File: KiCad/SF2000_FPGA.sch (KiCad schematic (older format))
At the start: 23 parts, among them J10 Conn_02x01, J11 Conn_02x01, J12 Conn_01x01, J3 Conn_02x03_Odd_Even, J4 Conn_02x01, J8 Conn_02x01, J9 Conn_02x01, U28 GW1N-UV9LQ144, U3 74LVC2G14, U8 T8Q144C3

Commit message: Fixed enumeration of single resistors references in ascending order
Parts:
- R3: renamed from R2; value 33Ω -> 33
- R4: renamed from R6; value 220 -> 330
- renumbered R11 to R10, R13 to R11, R12 to R5, R9 to R6, R4 to R8, R5 to R9
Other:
- moved on the sheet: R10, R11, R5, R6
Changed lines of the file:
@@
 P 7500 1850
 AR Path="/62517BB4" Ref="R?"  Part="1"
-AR Path="/620D263D/62517BB4" Ref="R4"  Part="1"
-F 0 "R4" H 7559 1896 50  0000 L CNN
+AR Path="/620D263D/62517BB4" Ref="R8"  Part="1"
+F 0 "R8" H 7559 1896 50  0000 L CNN
 F 1 "10k" H 7559 1805 50  0000 L CNN
 F 2 "Resistor_SMD:R_0805_2012Metric_Pad1.15x1.40mm_HandSolder" H 7500 1850 50  0001 C CNN
@@
 P 8000 2050
 AR Path="/62519236" Ref="R?"  Part="1"
-AR Path="/620D263D/62519236" Ref="R5"  Part="1"
-F 0 "R5" V 8100 2000 50  0000 L CNN
+AR Path="/620D263D/62519236" Ref="R9"  Part="1"
+F 0 "R9" V 8100 2000 50  0000 L CNN
 F 1 "10k" V 7900 2000 50  0000 L CNN
 F 2 "Resistor_SMD:R_0805_2012Metric_Pad1.15x1.40mm_HandSolder" H 8000 2050 50  0001 C CNN
@@
 P 9900 3050
 AR Path="/625C5BBC" Ref="R?"  Part="1"
-AR Path="/620D263D/625C5BBC" Ref="R6"  Part="1"
-F 0 "R6" V 10000 3000 50  0000 L CNN
-F 1 "220" V 9800 3000 50  0000 L CNN
+AR Path="/620D263D/625C5BBC" Ref="R4"  Part="1"
+F 0 "R4" V 10000 3000 50  0000 L CNN
+F 1 "330" V 9800 3000 50  0000 L CNN
 F 2 "Resistor_SMD:R_0805_2012Metric_Pad1.15x1.40mm_HandSolder" H 9900 3050 50  0001 C CNN
 F 3 "~" H 9900 3050 50  0001 C CNN
@@
 P -7250 4900
 AR Path="/6302BBCE" Ref="R?"  Part="1"
-AR Path="/620D263D/6302BBCE" Ref="R2"  Part="1"
-F 0 "R2" V -7350 4800 50  0000 L CNN
-F 1 "33Ω" V -7150 4850 50  0000 L CNN
+AR Path="/620D263D/6302BBCE" Ref="R3"  Part="1"
+F 0 "R3" V -7350 4800 50  0000 L CNN
+F 1 "33" V -7250 4850 50  0000 L CNN
 F 2 "Resistor_SMD:R_0805_2012Metric_Pad1.15x1.40mm_HandSolder" H -7250 4900 50  0001 C CNN
 F 3 "~" H -7250 4900 50  0001 C CNN
@@
 TDI
 NoConn ~ 7750 3200
-Text GLabel 10300 4050 3    50   Input ~ 0
+Text GLabel 10750 4050 3    50   Input ~ 0
 ACTIVE
-Text GLabel 10300 3850 1    50   Input ~ 0
-3V3
-$Comp
-L Device:R_Small R?
-U 1 1 63189641
-P 10300 3950
-AR Path="/63189641" Ref="R?"  Part="1"
-AR Path="/620D263D/63189641" Ref="R13"  Part="1"
-F 0 "R13" V 10400 3900 50  0000 L CNN
-F 1 "10k" V 10200 3900 50  0000 L CNN
-F 2 "Resistor_SMD:R_0805_2012Metric_Pad1.15x1.40mm_HandSolder" H 10300 3950 50  0001 C CNN
-F 3 "~" H 10300 3950 50  0001 C CNN
-	1    10300 3950
-	1    0    0    -1
-$EndComp
-Text GLabel 9950 3850 1    50   Input ~ 0
+Text GLabel 10750 3850 1    50   Input ~ 0
+3V3
+Text GLabel 9700 3850 1    50   Input ~ 0
 3V3
 $Comp
 L Device:R_Small R?
 U 1 1 6314ED20
-P 9950 3950
+P 9700 3950
 AR Path="/6314ED20" Ref="R?"  Part="1"
-AR Path="/620D263D/6314ED20" Ref="R12"  Part="1"
-F 0 "R12" V 10050 3900 50  0000 L CNN
-F 1 "10k" V 9850 3900 50  0000 L CNN
-F 2 "Resistor_SMD:R_0805_2012Metric_Pad1.15x1.40mm_HandSolder" H 9950 3950 50  0001 C CNN
-F 3 "~" H 9950 3950 50  0001 C CNN
-	1    9950 3950
-	1    0    0    -1
-$EndComp
-Text GLabel 9600 3850 1    50   Input ~ 0
-3V3
-$Comp
-L Device:R_Small R?
-U 1 1 68C712CB
-P 10650 3950
-AR Path="/68C712CB" Ref="R?"  Part="1"
-AR Path="/620D263D/68C712CB" Ref="R11"  Part="1"
-F 0 "R11" V 10750 3900 50  0000 L CNN
-F 1 "100k" V 10550 3850 50  0000 L CNN
-F 2 "Resistor_SMD:R_0805_2012Metric_Pad1.20x1.40mm_HandSolder" H 10650 3950 50  0001 C CNN
-F 3 "~" H 10650 3950 50  0001 C CNN
-	1    10650 3950
-	1    0    0    -1
-$EndComp
-Text GLabel 10650 3850 1    50   Input ~ 0
-3V3
-Text GLabel 10650 4050 3    50   Input ~ 0
+AR Path="/620D263D/6314ED20" Ref="R5"  Part="1"
+F 0 "R5" V 9800 3900 50  0000 L CNN
+F 1 "10k" V 9600 3900 50  0000 L CNN
+F 2 "Resistor_SMD:R_0805_2012Metric_Pad1.15x1.40mm_HandSolder" H 9700 3950 50  0001 C CNN
+F 3 "~" H 9700 3950 50  0001 C CNN
+	1    9700 3950
+	1    0    0    -1
+$EndComp
+Text GLabel 10050 3850 1    50   Input ~ 0
+3V3
+Text GLabel 10400 3850 1    50   Input ~ 0
+3V3
+Text GLabel 10400 4050 3    50   Input ~ 0
 CRESET_N
 Text GLabel -6750 5100 0    50   Input ~ 0
@@
 	10350 5600 10250 5600
 NoConn ~ -6750 5200
-Text GLabel 9600 4050 3    50   Input ~ 0
+Text GLabel 10050 4050 3    50   Input ~ 0
 JP2
 $Comp
 L Device:R_Small R?
 U 1 1 626987D6
-P 9600 3950
+P 10050 3950
 AR Path="/626987D6" Ref="R?"  Part="1"
-AR Path="/620D263D/626987D6" Ref="R9"  Part="1"
-F 0 "R9" V 9700 3900 50  0000 L CNN
-F 1 "10k" V 9500 3900 50  0000 L CNN
-F 2 "Resistor_SMD:R_0805_2012Metric_Pad1.15x1.40mm_HandSolder" H 9600 3950 50  0001 C CNN
-F 3 "~" H 9600 3950 50  0001 C CNN
-	1    9600 3950
+AR Path="/620D263D/626987D6" Ref="R6"  Part="1"
+F 0 "R6" V 10150 3900 50  0000 L CNN
+F 1 "10k" V 9950 3900 50  0000 L CNN
+F 2 "Resistor_SMD:R_0805_2012Metric_Pad1.15x1.40mm_HandSolder" H 10050 3950 50  0001 C CNN
+F 3 "~" H 10050 3950 50  0001 C CNN
+	1    10050 3950
 	1    0    0    -1
 $EndComp
@@
 Wire Wire Line
 	-7350 4900 -7350 5050
-Text GLabel 9950 4050 3    50   Input ~ 0
+Text GLabel 9700 4050 3    50   Input ~ 0
 SPI_SS
 Text GLabel 7750 3100 2    50   Input ~ 0
 SPI_SS
+$Comp
+L Device:R_Small R?
+U 1 1 63189641
+P 10750 3950
+AR Path="/63189641" Ref="R?"  Part="1"
+AR Path="/620D263D/63189641" Ref="R11"  Part="1"
+F 0 "R11" V 10850 3900 50  0000 L CNN
+F 1 "10k" V 10650 3900 50  0000 L CNN
+F 2 "Resistor_SMD:R_0805_2012Metric_Pad1.15x1.40mm_HandSolder" H 10750 3950 50  0001 C CNN
+F 3 "~" H 10750 3950 50  0001 C CNN
+	1    10750 3950
+	1    0    0    -1
+$EndComp
+$Comp
+L Device:R_Small R?
+U 1 1 68C712CB
+P 10400 3950
+AR Path="/68C712CB" Ref="R?"  Part="1"
+AR Path="/620D263D/68C712CB" Ref="R10"  Part="1"
+F 0 "R10" V 10500 3900 50  0000 L CNN
+F 1 "100k" V 10300 3850 50  0000 L CNN
+F 2 "Resistor_SMD:R_0805_2012Metric_Pad1.20x1.40mm_HandSolder" H 10400 3950 50  0001 C CNN
+F 3 "~" H 10400 3950 50  0001 C CNN
+	1    10400 3950
+	1    0    0    -1
+$EndComp
 $EndSCHEMATC

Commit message: Add TLV74312PDBV 1.2V voltage regulator, change C7 value to 2.2uF
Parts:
- renumbered U3 to U19
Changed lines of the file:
@@
 GND
 $Comp
-L SF2000:74LVC2G14 U3
+L SF2000:74LVC2G14 U19
 U 1 1 623FD973
 P 9250 2250
-F 0 "U3" H 9250 2765 50  0000 C CNN
+F 0 "U19" H 9250 2765 50  0000 C CNN
 F 1 "74LVC2G14" H 9250 2674 50  0000 C CNN
 F 2 "Package_SO:TSOP-6_1.65x3.05mm_P0.95mm" H 9750 3200 50  0001 C CNN

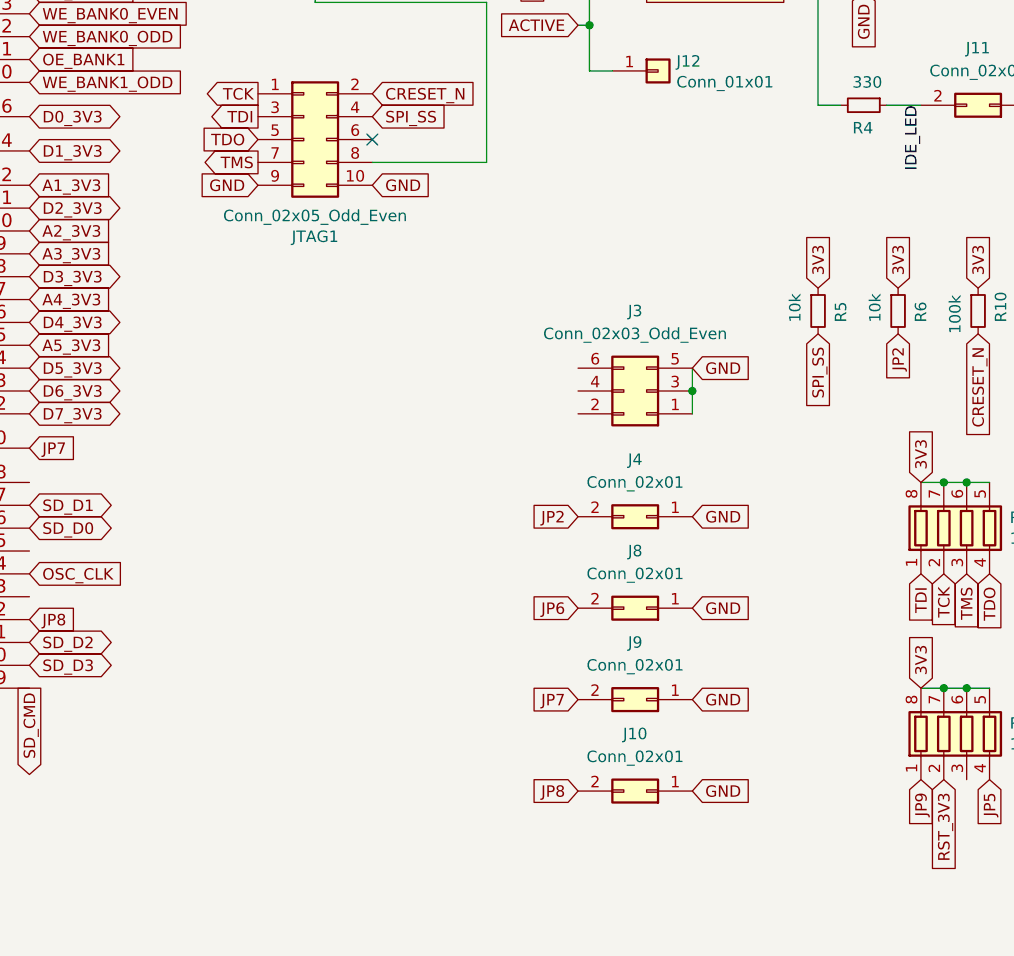
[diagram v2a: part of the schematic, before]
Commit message: Add SPI NOR Flash 8 Mbit in SOIC-8 package (AT25SF081B-SSH)
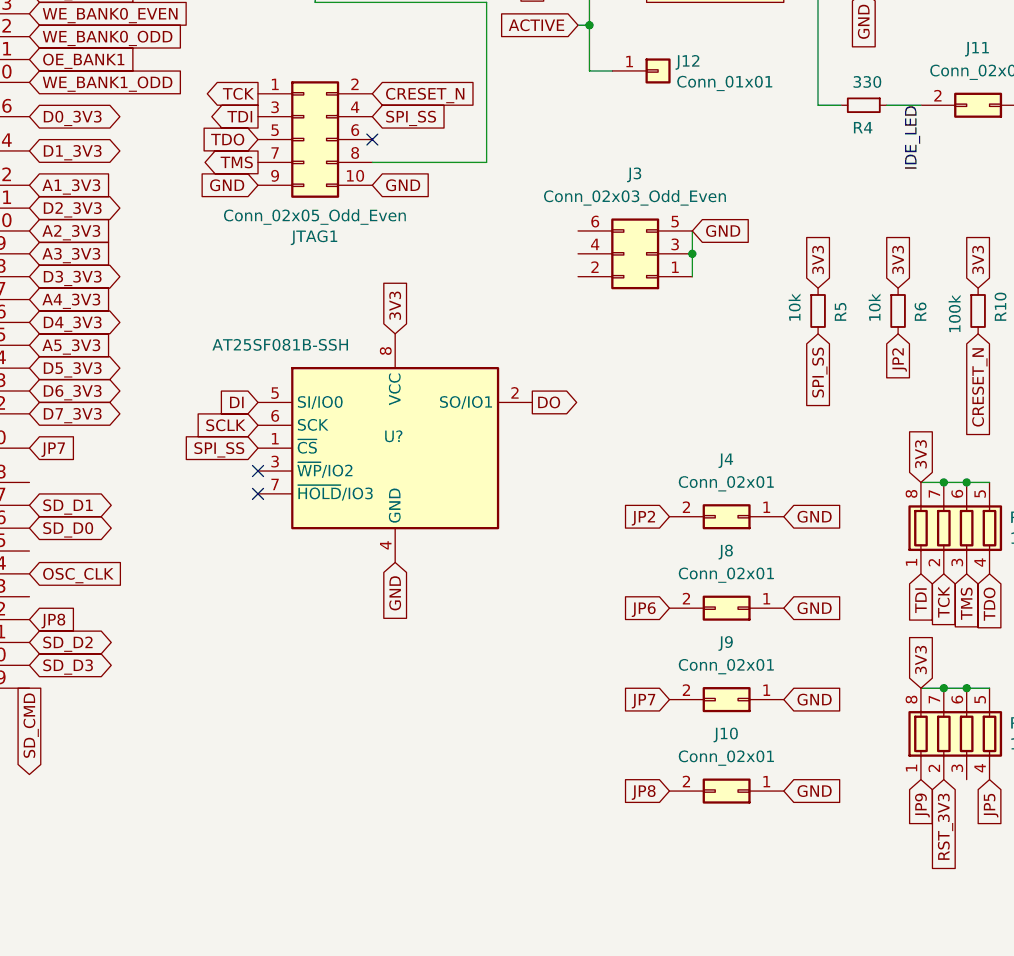
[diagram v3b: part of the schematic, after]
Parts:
- added U?: AT25SF081B-SSH, Package_SO:SOIC-8_3.9x4.9mm_P1.27mm, symbol Memory_Flash:AT25SF081-SSHD-X
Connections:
- net 3V3: now also U?.8 (VCC)
- net DI: now also U?.5 (SI/IO0)
- net DO: now also U?.2 (SO/IO1)
- net GND: now also U?.4 (GND)
- net SCLK: now also U?.6 (SCK)
- net SPI_SS: now also U?.1 (~CS)
- no-connect marks 3 -> 5
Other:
- moved on the sheet: J10, J3, J4, J8, J9
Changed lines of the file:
@@
 Text GLabel -6750 3200 0    50   Input ~ 0
 JP1
-Text GLabel 8650 4850 0    50   Input ~ 0
+Text GLabel 9050 4850 0    50   Input ~ 0
 JP2
 $Comp
@@
 L Connector_Generic:Conn_02x03_Odd_Even J3
 U 1 1 62704BD7
-P 8950 4300
-F 0 "J3" H 9000 3950 50  0000 C CNN
-F 1 "Conn_02x03_Odd_Even" H 9000 4050 50  0000 C CNN
-F 2 "Connector_PinHeader_2.00mm:PinHeader_2x03_P2.00mm_Vertical" H 8950 4300 50  0001 C CNN
-F 3 "~" H 8950 4300 50  0001 C CNN
-	1    8950 4300
+P 8950 3700
+F 0 "J3" H 9000 3350 50  0000 C CNN
+F 1 "Conn_02x03_Odd_Even" H 9000 3450 50  0000 C CNN
+F 2 "Connector_PinHeader_2.00mm:PinHeader_2x03_P2.00mm_Vertical" H 8950 3700 50  0001 C CNN
+F 3 "~" H 8950 3700 50  0001 C CNN
+	1    8950 3700
 	-1   0    0    1
 $EndComp
 Wire Wire Line
-	9150 4200 9150 4300
-Connection ~ 9150 4300
-Wire Wire Line
-	9150 4300 9150 4400
-Text GLabel 9150 4200 2    50   Input ~ 0
+	9150 3600 9150 3700
+Connection ~ 9150 3700
+Wire Wire Line
+	9150 3700 9150 3800
+Text GLabel 9150 3600 2    50   Input ~ 0
 GND
 $Comp
 L Connector_Generic:Conn_02x01 J4
 U 1 1 6276C760
-P 8950 4850
-F 0 "J4" H 9000 4600 50  0000 C CNN
-F 1 "Conn_02x01" H 9000 4700 50  0000 C CNN
-F 2 "Connector_PinHeader_2.00mm:PinHeader_2x01_P2.00mm_Vertical" H 8950 4850 50  0001 C CNN
-F 3 "~" H 8950 4850 50  0001 C CNN
-	1    8950 4850
+P 9350 4850
+F 0 "J4" H 9400 4600 50  0000 C CNN
+F 1 "Conn_02x01" H 9400 4700 50  0000 C CNN
+F 2 "Connector_PinHeader_2.00mm:PinHeader_2x01_P2.00mm_Vertical" H 9350 4850 50  0001 C CNN
+F 3 "~" H 9350 4850 50  0001 C CNN
+	1    9350 4850
 	-1   0    0    1
 $EndComp
-Text GLabel 9150 4850 2    50   Input ~ 0
+Text GLabel 9550 4850 2    50   Input ~ 0
 GND
 Text GLabel 9700 2050 2    50   Output ~ 0
@@
 L Connector_Generic:Conn_02x01 J9
 U 1 1 62127717
-P 8950 5650
-F 0 "J9" H 9000 5400 50  0000 C CNN
-F 1 "Conn_02x01" H 9000 5500 50  0000 C CNN
-F 2 "Connector_PinHeader_2.00mm:PinHeader_2x01_P2.00mm_Vertical" H 8950 5650 50  0001 C CNN
-F 3 "~" H 8950 5650 50  0001 C CNN
-	1    8950 5650
+P 9350 5650
+F 0 "J9" H 9400 5400 50  0000 C CNN
+F 1 "Conn_02x01" H 9400 5500 50  0000 C CNN
+F 2 "Connector_PinHeader_2.00mm:PinHeader_2x01_P2.00mm_Vertical" H 9350 5650 50  0001 C CNN
+F 3 "~" H 9350 5650 50  0001 C CNN
+	1    9350 5650
 	-1   0    0    1
 $EndComp
-Text GLabel 9150 5650 2    50   Input ~ 0
-GND
-Text GLabel 8650 5650 0    50   Input ~ 0
+Text GLabel 9550 5650 2    50   Input ~ 0
+GND
+Text GLabel 9050 5650 0    50   Input ~ 0
 JP7
 $Comp
 L Connector_Generic:Conn_02x01 J10
 U 1 1 62132436
-P 8950 6050
-F 0 "J10" H 9000 5800 50  0000 C CNN
-F 1 "Conn_02x01" H 9000 5900 50  0000 C CNN
-F 2 "Connector_PinHeader_2.00mm:PinHeader_2x01_P2.00mm_Vertical" H 8950 6050 50  0001 C CNN
-F 3 "~" H 8950 6050 50  0001 C CNN
-	1    8950 6050
+P 9350 6050
+F 0 "J10" H 9400 5800 50  0000 C CNN
+F 1 "Conn_02x01" H 9400 5900 50  0000 C CNN
+F 2 "Connector_PinHeader_2.00mm:PinHeader_2x01_P2.00mm_Vertical" H 9350 6050 50  0001 C CNN
+F 3 "~" H 9350 6050 50  0001 C CNN
+	1    9350 6050
 	-1   0    0    1
 $EndComp
-Text GLabel 9150 6050 2    50   Input ~ 0
-GND
-Text GLabel 8650 6050 0    50   Input ~ 0
+Text GLabel 9550 6050 2    50   Input ~ 0
+GND
+Text GLabel 9050 6050 0    50   Input ~ 0
 JP8
 Text GLabel 6250 5300 2    50   Input ~ 0
@@
 Text GLabel 4800 6000 3    50   Output ~ 0
 ROM_B2
-Text GLabel 8650 5250 0    50   Input ~ 0
+Text GLabel 9050 5250 0    50   Input ~ 0
 JP6
 $Comp
 L Connector_Generic:Conn_02x01 J8
 U 1 1 621772F2
-P 8950 5250
-F 0 "J8" H 9000 5000 50  0000 C CNN
-F 1 "Conn_02x01" H 9000 5100 50  0000 C CNN
-F 2 "Connector_PinHeader_2.00mm:PinHeader_2x01_P2.00mm_Vertical" H 8950 5250 50  0001 C CNN
-F 3 "~" H 8950 5250 50  0001 C CNN
-	1    8950 5250
+P 9350 5250
+F 0 "J8" H 9400 5000 50  0000 C CNN
+F 1 "Conn_02x01" H 9400 5100 50  0000 C CNN
+F 2 "Connector_PinHeader_2.00mm:PinHeader_2x01_P2.00mm_Vertical" H 9350 5250 50  0001 C CNN
+F 3 "~" H 9350 5250 50  0001 C CNN
+	1    9350 5250
 	-1   0    0    1
 $EndComp
-Text GLabel 9150 5250 2    50   Input ~ 0
+Text GLabel 9550 5250 2    50   Input ~ 0
 GND
 $Comp
@@
 	1    0    0    -1
 $EndComp
+$Comp
+L Memory_Flash:AT25SF081-SSHD-X U?
+U 1 1 6925ADB2
+P 7850 4550
+F 0 "U?" H 7800 4600 50  0000 L CNN
+F 1 "AT25SF081B-SSH" H 7050 5000 50  0000 L CNN
+F 2 "Package_SO:SOIC-8_3.9x4.9mm_P1.27mm" H 7850 3950 50  0001 C CNN
+F 3 "https://www.mouser.com/ProductDetail/988-AT25SF081-SSH-B" H 7850 4550 50  0001 C CNN
+	1    7850 4550
+	1    0    0    -1
+$EndComp
+NoConn ~ 7250 4650
+NoConn ~ 7250 4750
+Text GLabel 7850 4050 1    50   Input ~ 0
+3V3
+Text GLabel 7250 4550 0    50   Input ~ 0
+SPI_SS
+Text GLabel 7250 4450 0    50   Input ~ 0
+SCLK
+Text GLabel 7850 5050 3    50   Input ~ 0
+GND
+Text GLabel 7250 4350 0    50   Input ~ 0
+DI
+Text GLabel 8450 4350 2    50   Output ~ 0
+DO
 $EndSCHEMATC
